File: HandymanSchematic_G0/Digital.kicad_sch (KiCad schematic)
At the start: 42 parts, among them J1 SWD Header, J2 PWR, J3 JACKS, J4 FOOTSWITCH, J5 ScopeGroundLoop, Q3 2N7002, Q4 2N7002, SW1 RST, SW2 BYP, U4 STM32G030F6P6, U5 AMS1117, U6 SSD1306, Y1 32.768kHZ

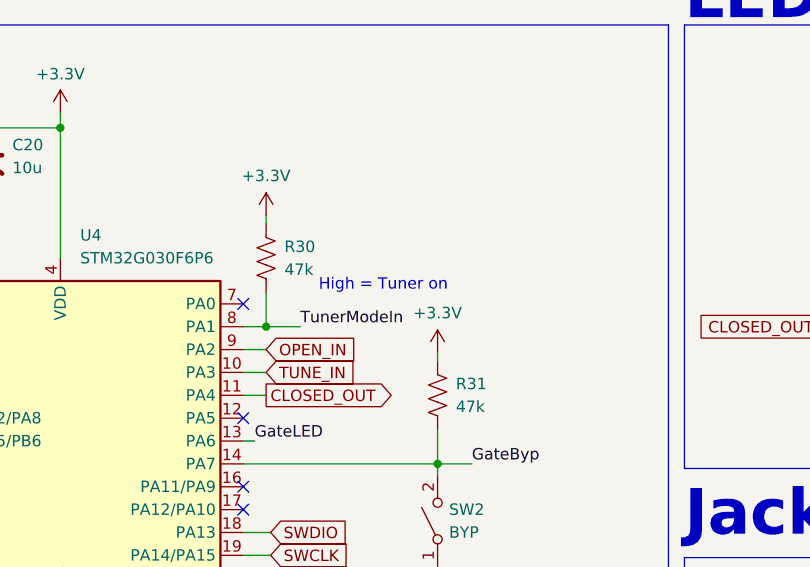
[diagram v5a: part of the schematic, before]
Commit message: mode switching handling
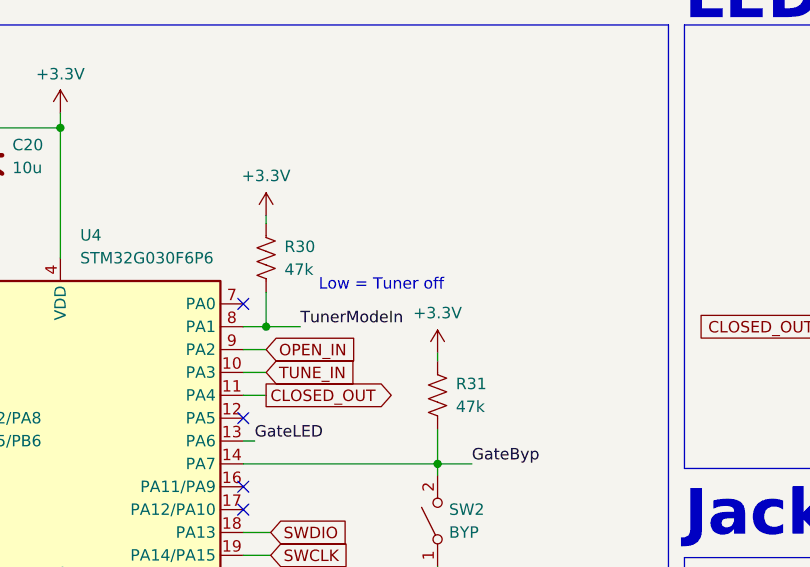
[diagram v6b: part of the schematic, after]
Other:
- note added: "Low = Tuner off"
- note removed: "High = Tuner on"
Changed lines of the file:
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@@
 		)
 	)
-	(text "High = Tuner on"
+	(text "Low = Tuner off"
 		(exclude_from_sim no)
 		(at 108.712 56.388 0)

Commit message: rough layout
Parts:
- removed TP8: 3v3, TestPoint:TestPoint_THTPad_D2.0mm_Drill1.0mm_VAL, symbol Connector:TestPoint
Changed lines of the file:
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@@
 	(wire
 		(pts
-			(xy 220.98 143.51) (xy 220.98 141.732)
-		)
-		(stroke
-			(width 0)
-			(type default)
-		)
-	)
-	(wire
-		(pts
 			(xy 102.87 57.15) (xy 102.87 60.96)
 		)
@@
 	(wire
 		(pts
-			(xy 209.55 140.97) (xy 209.55 143.51)
-		)
-		(stroke
-			(width 0)
-			(type default)
-		)
-	)
-	(wire
-		(pts
 			(xy 48.26 83.82) (xy 48.26 85.09)
 		)
@@
 	(wire
 		(pts
-			(xy 209.55 143.51) (xy 220.98 143.51)
-		)
-		(stroke
-			(width 0)
-			(type default)
-		)
-	)
-	(wire
-		(pts
 			(xy 167.64 60.96) (xy 167.64 63.5)
 		)
@@
 	)
 	(symbol
-		(lib_id "Connector:TestPoint")
-		(at 209.55 140.97 0)
-		(unit 1)
-		(exclude_from_sim no)
-		(in_bom no)
-		(on_board yes)
-		(dnp no)
-		(fields_autoplaced yes)
-		(property "Reference" "TP8"
-			(at 211.582 136.3979 0)
-			(effects
-				(font
-					(size 1.27 1.27)
-				)
-				(justify left)
-			)
-		)
-		(property "Value" "3v3"
-			(at 211.582 138.9379 0)
-			(effects
-				(font
-					(size 1.27 1.27)
-				)
-				(justify left)
-			)
-		)
-		(property "Footprint" "TestPoint:TestPoint_THTPad_D2.0mm_Drill1.0mm_VAL"
-			(at 214.63 140.97 0)
-			(effects
-				(font
-					(size 1.27 1.27)
-				)
-				(hide yes)
-			)
-		)
-		(property "Datasheet" "~"
-			(at 214.63 140.97 0)
-			(effects
-				(font
-					(size 1.27 1.27)
-				)
-				(hide yes)
-			)
-		)
-		(property "Description" "test point"
-			(at 209.55 140.97 0)
-			(effects
-				(font
-					(size 1.27 1.27)
-				)
-				(hide yes)
-			)
-		)
-		(pin "1"
-		)
-		(instances
-			(project "HandymanSchematic_G0"
-				(path "/bc3da82e-d0a7-49a6-b9ec-ecd2040670ff/887caaef-7a77-44c5-aff2-1e54e61c47e4"
-					(reference "TP8")
-					(unit 1)
-				)
-			)
-		)
-	)
-	(symbol
 		(lib_id "power:GND")
 		(at 80.01 94.742 0)
@@
 					(unit 1)
 				)
-			)
-		)
-	)
-	(symbol
-		(lib_name "+3.3V_1")
-		(lib_id "power:+3.3V")
-		(at 220.98 141.732 0)
-		(unit 1)
-		(exclude_from_sim no)
-		(in_bom yes)
-		(on_board yes)
-		(dnp no)
-		(fields_autoplaced yes)
-		(property "Reference" "#PWR053"
-			(at 220.98 145.542 0)
-			(effects
-				(font
-					(size 1.27 1.27)
-				)
-				(hide yes)
-			)
-		)
-		(property "Value" "+3.3V"
-			(at 220.98 136.398 0)
-			(effects
-				(font
-					(size 1.27 1.27)
-				)
-			)
-		)
-		(property "Footprint" ""
-			(at 220.98 141.732 0)
-			(effects
-				(font
-					(size 1.27 1.27)
-				)
-				(hide yes)
-			)
-		)
-		(property "Datasheet" ""
-			(at 220.98 141.732 0)
-			(effects
-				(font
-					(size 1.27 1.27)
-				)
-				(hide yes)
-			)
-		)
-		(property "Description" "Power symbol creates a global label with name \"+3.3V\""
-			(at 220.98 141.732 0)
-			(effects
-				(font
-					(size 1.27 1.27)
-				)
-				(hide yes)
-			)
-		)
-		(pin "1"
-		)
-		(instances
-			(project "HandymanSchematic_G0"
-				(path "/bc3da82e-d0a7-49a6-b9ec-ecd2040670ff/887caaef-7a77-44c5-aff2-1e54e61c47e4"
-					(reference "#PWR053")
-					(unit 1)
-				)

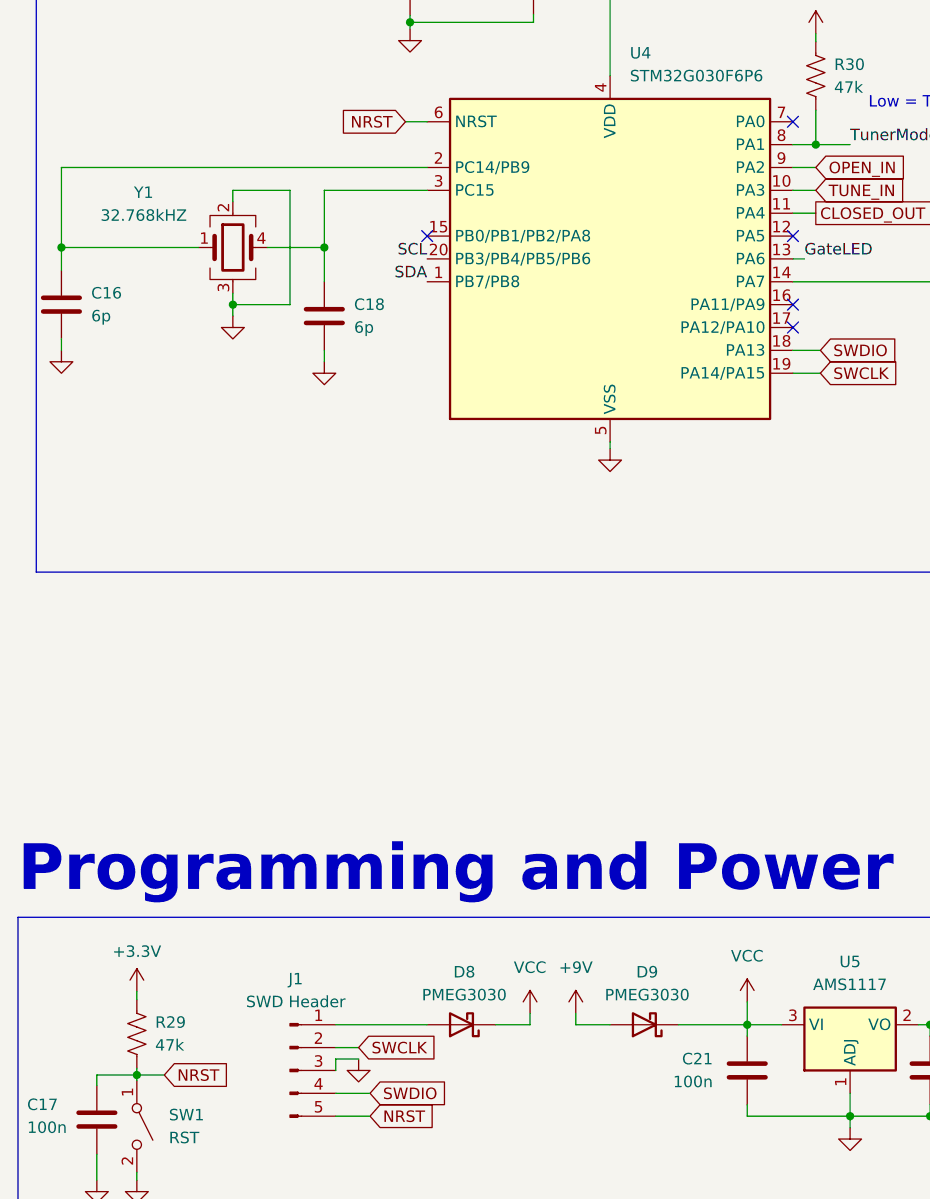
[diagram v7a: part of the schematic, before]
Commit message: removed unused components
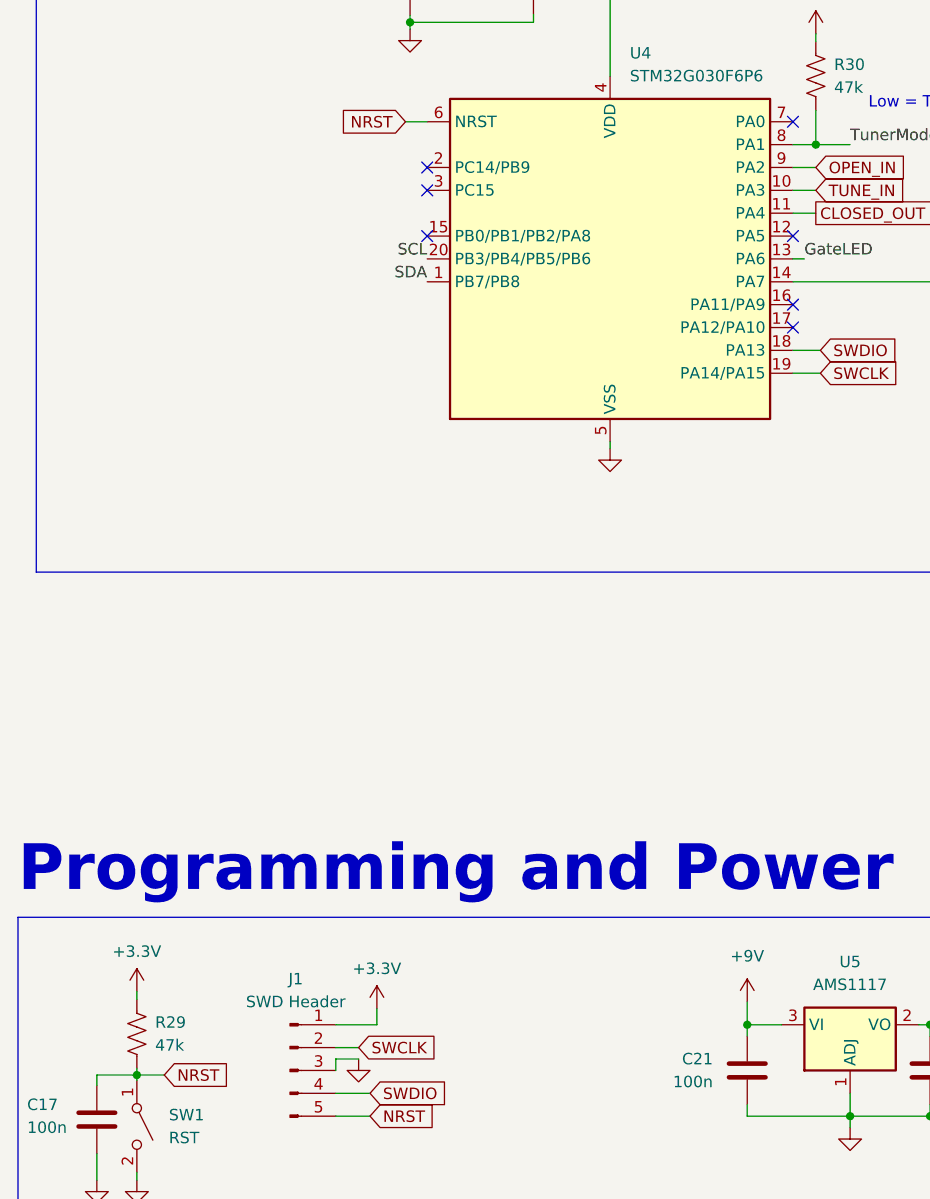
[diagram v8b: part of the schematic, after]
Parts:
- removed C16, C18: 6p, Capacitor_SMD:C_0805_2012Metric, symbol Device:C
- removed D8, D9: PMEG3030, Diode_SMD:D_SOD-123, symbol Device:D_Schottky
- removed Y1: 32.768kHZ, Crystal:Crystal_SMD_SeikoEpson_MC306-4Pin_8.0x3.2mm, symbol Device:Crystal_GND23
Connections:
- net VCC is gone; now on net +9V: C21.2, U5.3 (VI)
- net +3.3V: now also J1.1 (Pin_1)
- no-connect marks 5 -> 7
